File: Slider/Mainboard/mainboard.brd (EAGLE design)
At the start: 146 x 76 mm, 61 parts, among them IC1 7805TV, IC2 33CV, IC3 LM358, Q1 16MHz, SW1 MS MOT1, SW2 MS MOT2, T1 BC337, T2 BC337, U1 ATMEGA328P_PDIP, U2 MAX232PTH

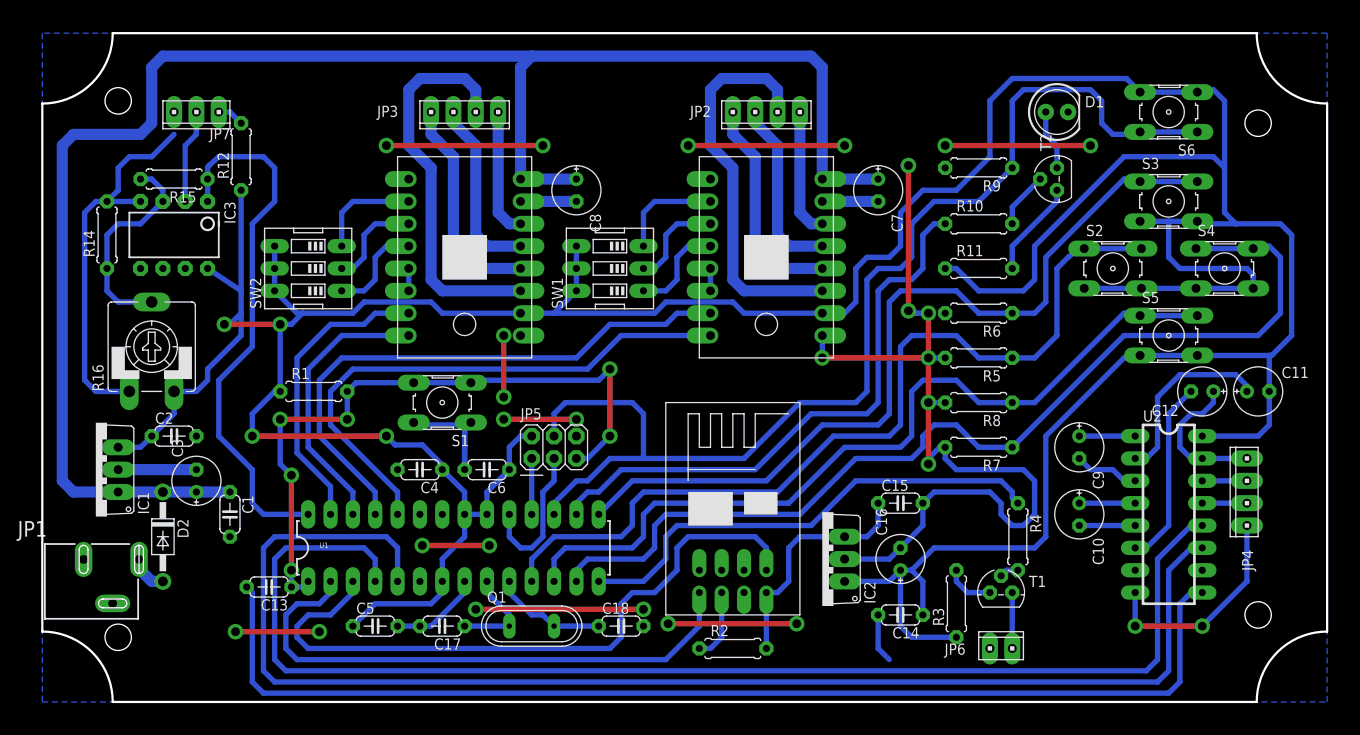
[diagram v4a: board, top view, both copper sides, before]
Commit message: added milling layer to board
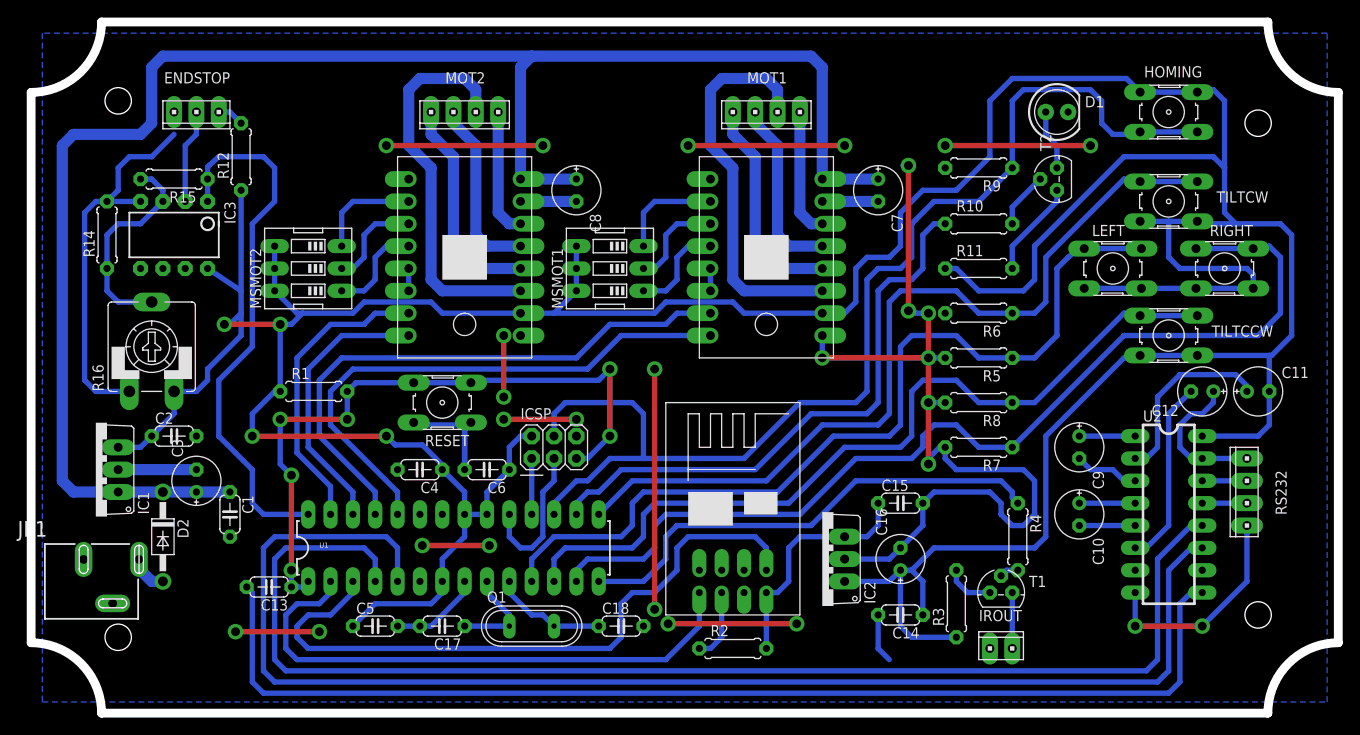
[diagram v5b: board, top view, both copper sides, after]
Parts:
- ENDSTOP: value ENDSTOP -> CONNECTOR
- HOMING: value HOMING -> SWITCH
- ICSP: value ICSP -> CONNECTOR
- IROUT: value IR -> CONNECTOR
- LEFT: value LEFT -> SWITCH
- MOT1: value MOT1 -> CONNECTOR
- MOT2: value MOT2 -> CONNECTOR
- MSMOT1: value MS MOT1 -> DIP SWITCH
- MSMOT2: value MS MOT2 -> DIP SWITCH
- RESET: value RESET -> SWITCH
- RIGHT: value RIGHT -> SWITCH
- RS232: value RS232 -> CONNECTOR
- TILTCCW: value TILT CCW -> SWITCH
- TILTCW: value TILT CW -> SWITCH
- renumbered JP2 to MOT1, JP3 to MOT2, JP4 to RS232, JP5 to ICSP, JP6 to IROUT, JP7 to ENDSTOP, S1 to RESET, S2 to LEFT, S3 to TILTCW, S4 to RIGHT, S5 to TILTCCW, S6 to HOMING, SW1 to MSMOT1, SW2 to MSMOT2, U$1 to U3, U$2 to U4, U$3 to U5
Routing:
- net GND: track 339.6 -> 347.9 mm
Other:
- board size 146 x 76 mm -> 148.5 x 78.5 mm
